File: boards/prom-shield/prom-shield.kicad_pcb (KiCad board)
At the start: 2 copper layers, 68.6 x 53.3 mm, 17 parts, among them J1 Analog, J2 Power, J3 Digital/PWM, J4 Digital/PWM, U1 28C256, U2 74HC595, U3 74HC595

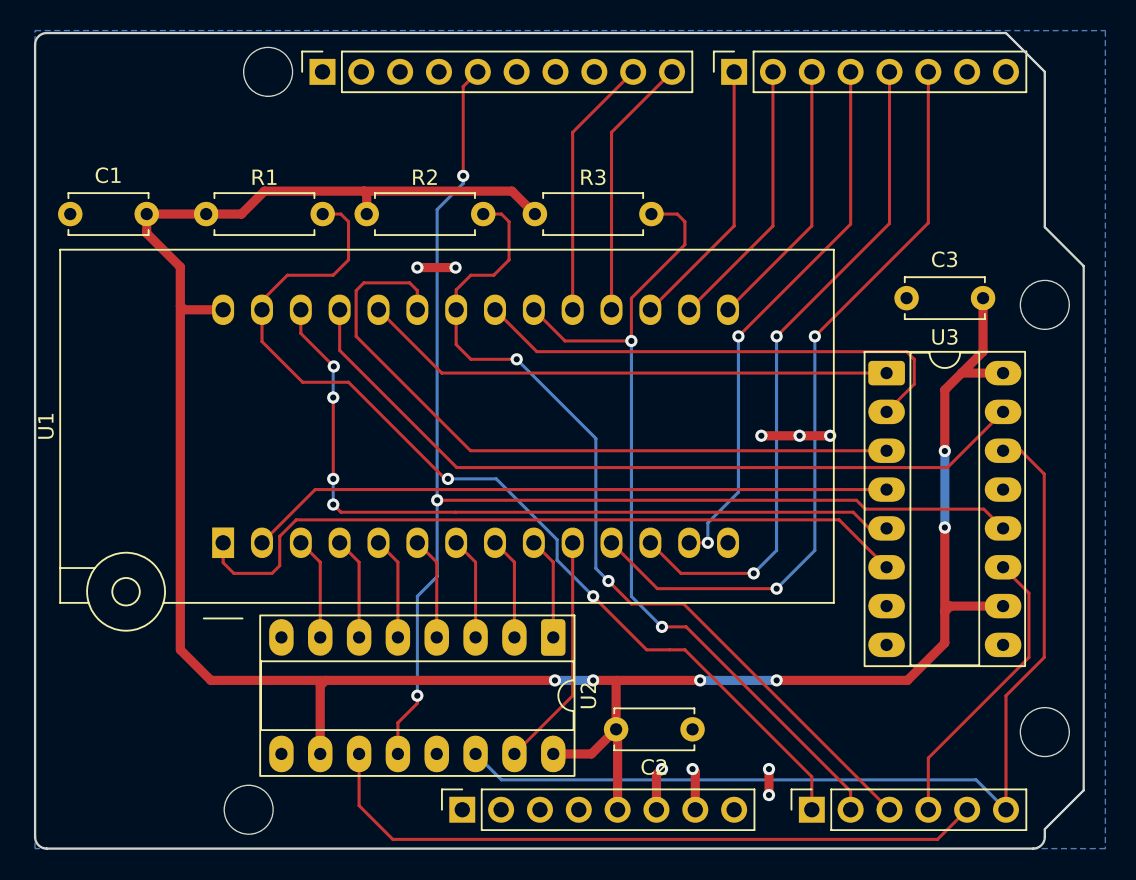
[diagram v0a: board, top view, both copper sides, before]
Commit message: Small routing tweaks to ROM programmer PCB
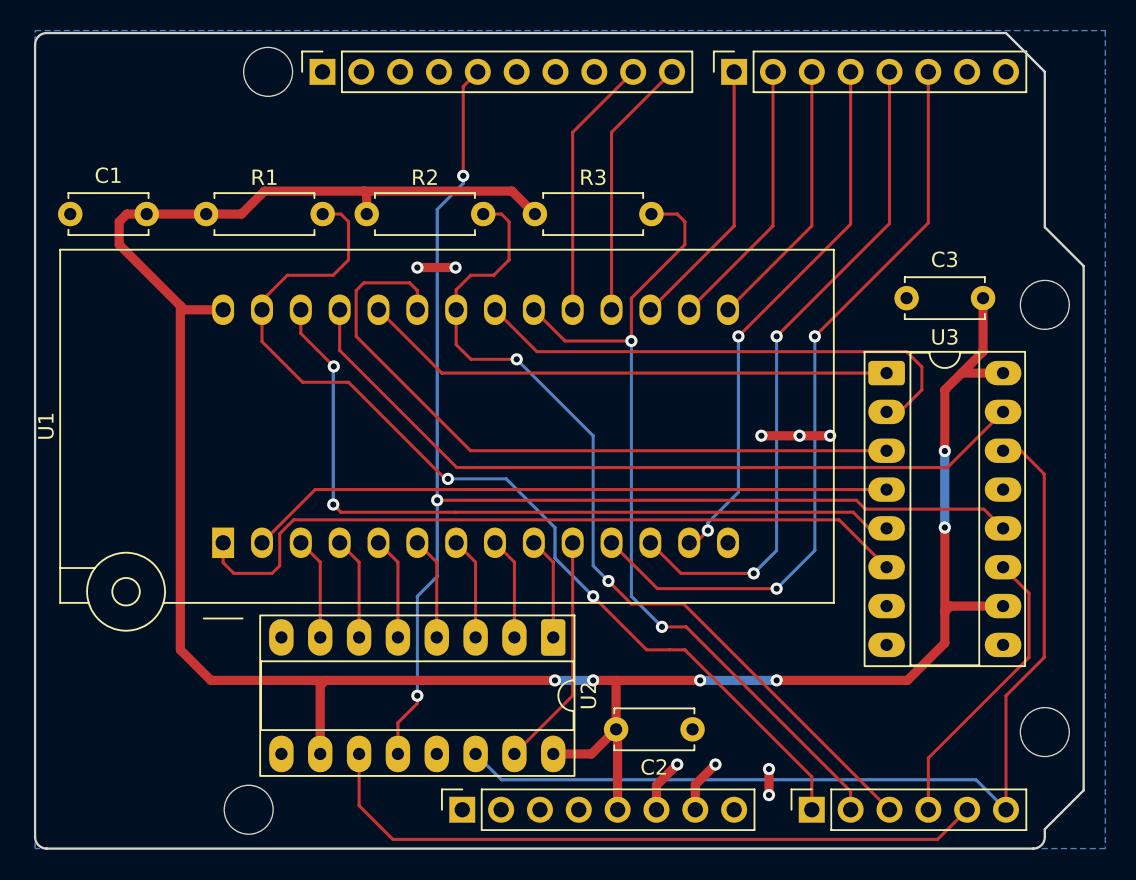
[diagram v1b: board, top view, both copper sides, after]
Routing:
- net VCC: track 160.9 -> 163.1 mm
- net GND: track 14.2 -> 15.7 mm
- net /A10: track 33.0 -> 33.9 mm
- net /A13: vias 4 -> 2

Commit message: New revision of PROM board
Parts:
- removed MH1, MH2, MH3, MH4: MountingHole_3.2mm, Arduino_MountingHole:MountingHole_3.2mm
- added G***: LOGO, custom:qr, F.Cu at (106.2, 87.8)
- moved R2 13.4 mm to (134.6, 54.8), turned to 180 degrees
- moved R3 13.4 mm to (145.6, 54.8), turned to 180 degrees
- moved R1 13.2 mm to (123.8, 54.8), turned to 180 degrees
- moved C3 13.1 mm to (163.8, 52.8), turned to -90 degrees
- moved U3 7.81 mm to (156.2, 61.1)
- moved C1 6.82 mm to (108.0, 54.8)
- moved U2 4.12 mm to (137.9, 85.2)
- moved U1 3.82 mm to (113.0, 76.2)
- moved C2 3.30 mm to (146.2, 92.8)
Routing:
- net VCC: track 163.1 -> 183.8 mm, vias 6 -> 2
- net /RCLK: track 84.8 -> 99.3 mm, vias 3 -> 1
- net /A11: track 46.5 -> 34.8 mm, vias 0 -> 1
- net /~{WE}: track 64.9 -> 76.0 mm
- net /A10: track 33.9 -> 26.5 mm
- net /~{CE}: track 56.4 -> 63.7 mm
- net /USR_SRCLK: track 19.3 -> 25.9 mm
- net /A8: track 50.7 -> 45.3 mm
- net /A12: track 42.3 -> 47.2 mm, vias 0 -> 1
- net /D0: track 50.0 -> 45.1 mm, vias 2 -> 1
- net /SER: track 62.5 -> 67.3 mm
- net /A14: track 48.9 -> 44.2 mm
- net /A0: track 15.4 -> 19.8 mm
- net /D2: track 35.4 -> 31.1 mm, vias 2 -> 0
- net /D1: track 44.1 -> 39.9 mm, vias 2 -> 1
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- added copper zone on F.Cu, net GND
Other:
- board text added: "Arduino UNO"
- board text added: "Dragos B."
- board text added: "For"
- board text added: "PROM Shield"
- board text added: "Rev. B"

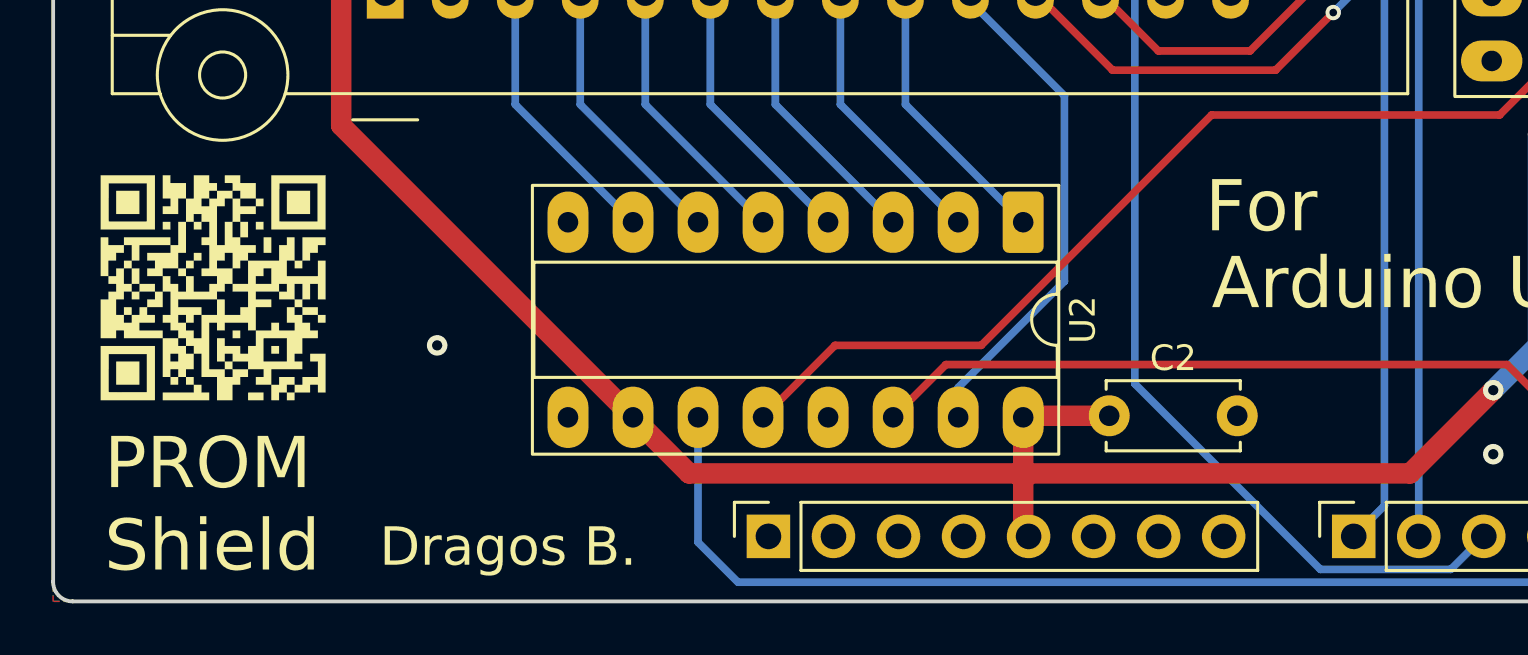
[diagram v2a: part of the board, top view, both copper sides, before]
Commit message: Fixed QR code library linking
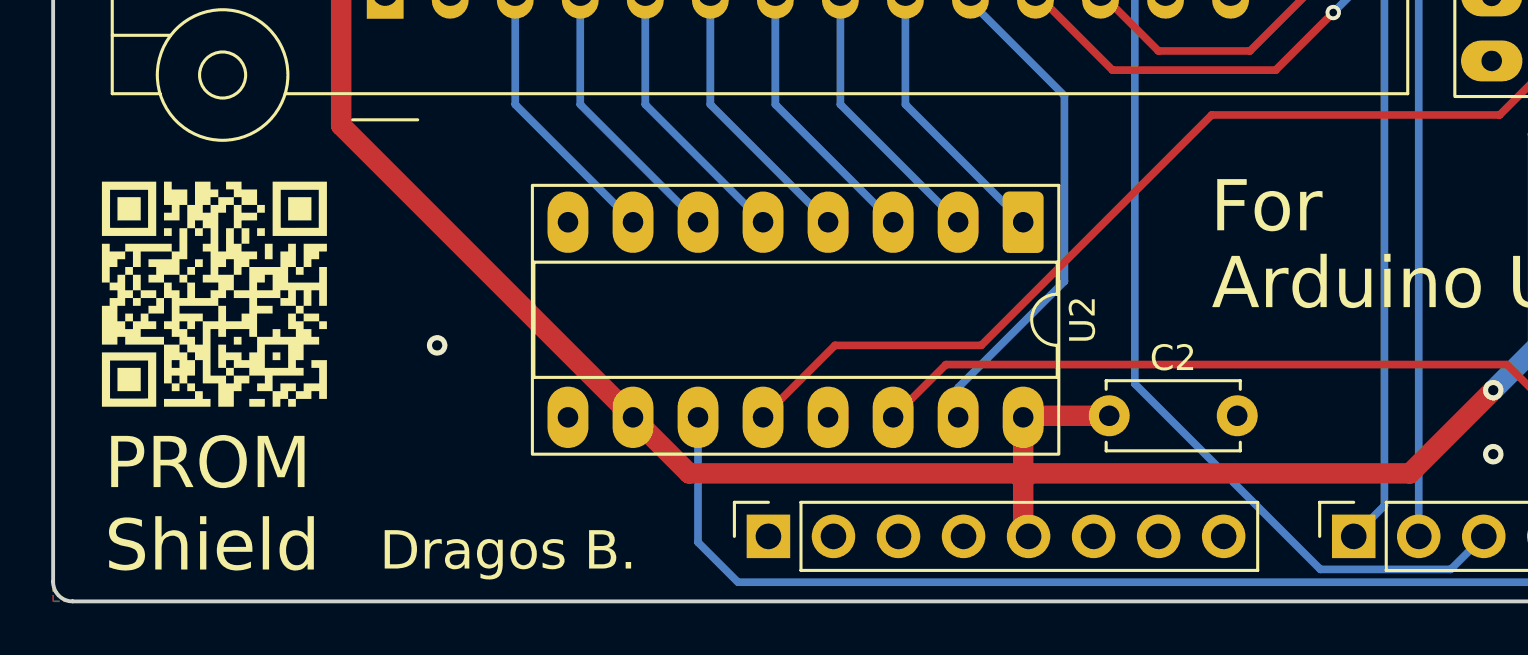
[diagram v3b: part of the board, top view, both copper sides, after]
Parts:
- removed the G*** at (106.2, 87.8)
- added G***: LOGO, code:qr, F.Cu at (106.3, 88.0)
